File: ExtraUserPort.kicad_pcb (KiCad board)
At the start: 2 copper layers, 60.8 x 99.9 mm, 35 parts, among them CN1 EXPANSION_PORT, CN2 ALMOST_USERPORT, CN3 DB9_MALE, J1 ATTENTION_IN, J2 TAPE_IN, U1 GAL20V8, U102 74LS652, U2 MOS_6529, U3 MOS_6551_ACIA, U4 MAX238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

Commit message: wip
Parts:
- moved JP4 0.61 mm to (136.0, 90.7), turned to 0 degrees
- moved J2 0.13 mm to (129.8, 93.0)
- renumbered C5 to C4, C9 to C5
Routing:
- net /pc2: track 90.1 -> 92.8 mm
- net /pc3: track 65.1 -> 66.4 mm
- net /pc0: track 68.6 -> 69.5 mm
- net Net-(CN2-Pad9): track 30.4 -> 30.9 mm
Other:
- board text added: "↓ 6529 / 74652 ↑"
- board text removed: "↑6529 ↓74652"

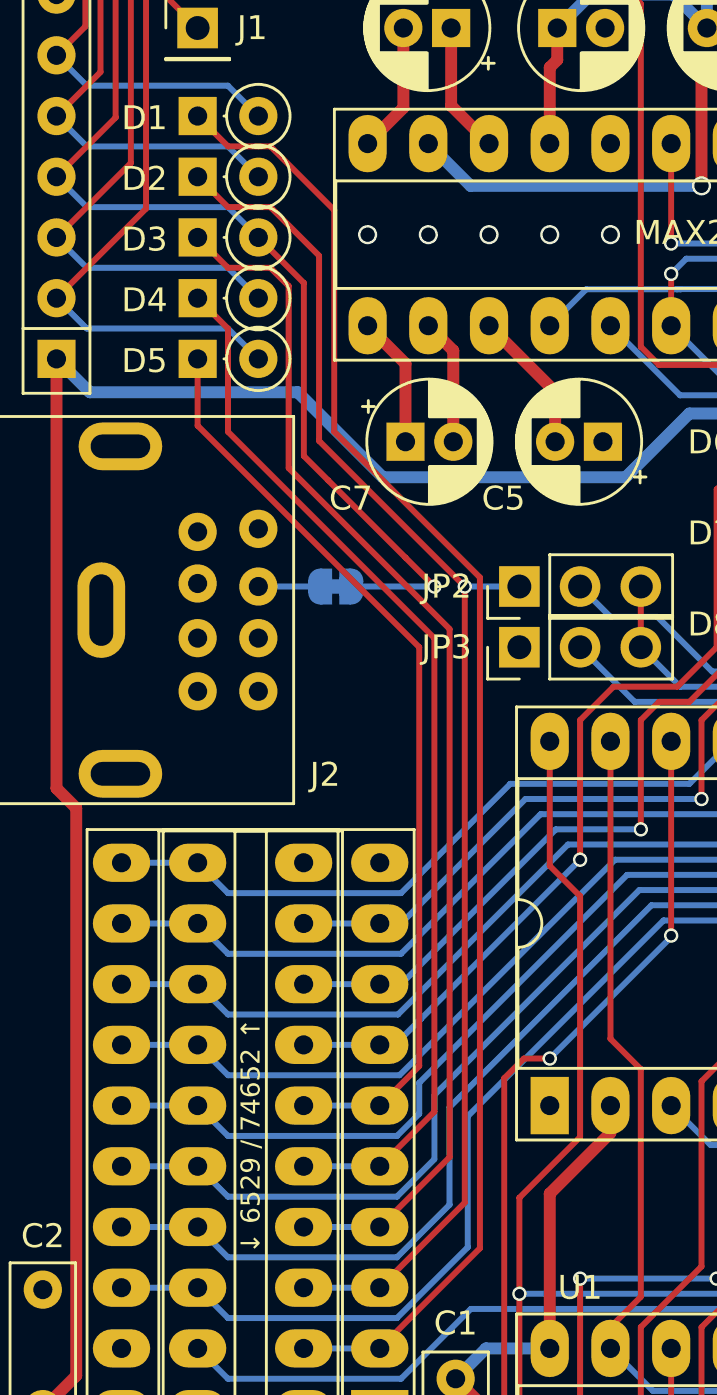
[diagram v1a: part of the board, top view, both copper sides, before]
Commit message: Move /CTS to PC2
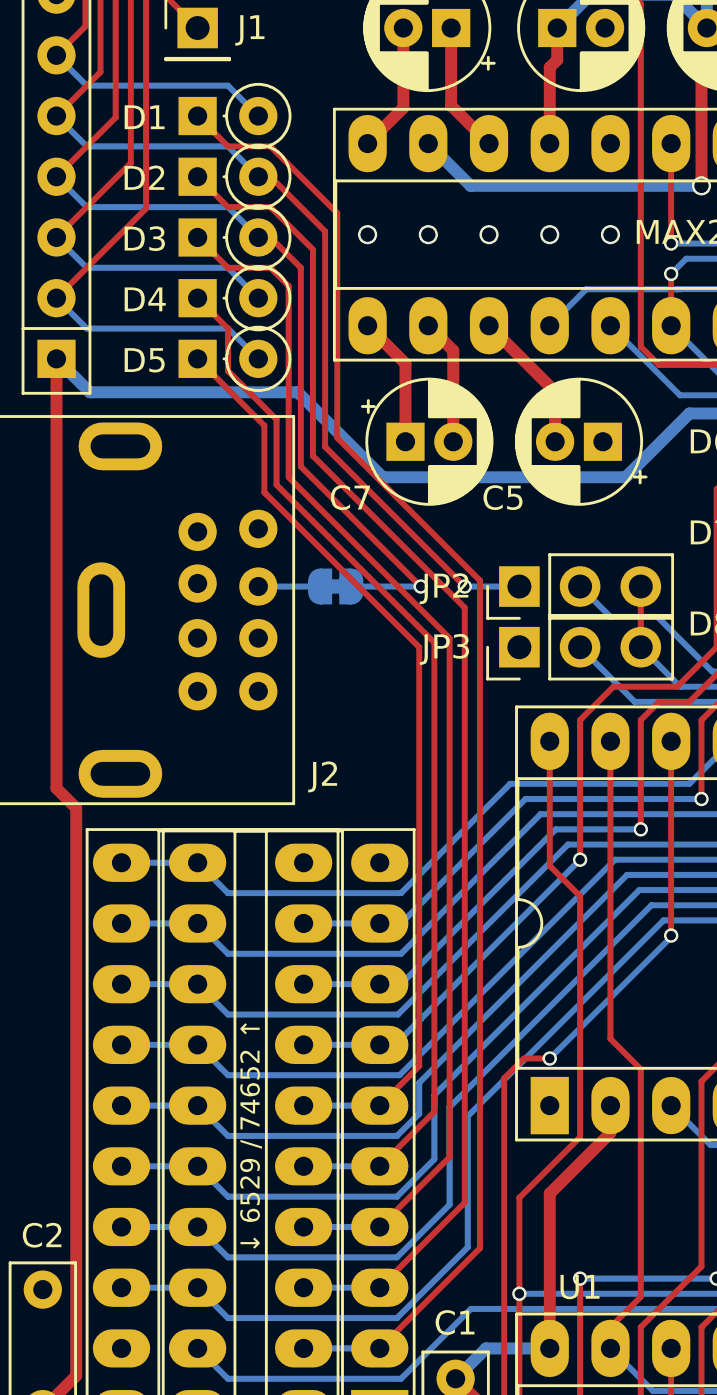
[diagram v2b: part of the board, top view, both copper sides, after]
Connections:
- JP2 pad 1: /p1 -> /pc1
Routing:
- net /pc1: track 47.4 -> 70.7 mm, vias 3 -> 4
- net /p1: track 59.1 -> 56.8 mm, vias 1 -> 0
- net /pc2: track 92.8 -> 92.3 mm

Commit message: Almost ready for prototypes
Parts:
- removed JP4: JMP_CASS_SENSE, Jumper:SolderJumper-2_P1.3mm_Bridged_RoundedPad1.0x1.5mm
- added R4: 1k, Resistor_THT:R_Axial_DIN0207_L6.3mm_D2.5mm_P2.54mm_Vertical, F.Cu at (156.3, 85.6)
- added R5: 1k, Resistor_THT:R_Axial_DIN0207_L6.3mm_D2.5mm_P2.54mm_Vertical, F.Cu at (160.1, 88.1)
- added V0: LOGO, ExtraUserPort:logo, F.Cu at (132.6, 135.6)
- added V1: CC-BY-NC-SA, ExtraUserPort:cc_by_nc_sa, B.Cu at (130.3, 135.8)
- moved D6 3.43 mm to (153.8, 88.1)
- moved D7 2.16 mm to (153.8, 90.7)
- moved R2 2.16 mm to (160.1, 90.7)
- moved D8 0.89 mm to (153.8, 93.2)
- moved R3 0.89 mm to (160.1, 93.2)
- moved R1 0.89 mm to (160.1, 85.6)
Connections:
- JP2 pad 1: /pc1 -> Net-(JP2-Pad1)
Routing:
- net /pc1: track 70.7 -> 91.9 mm
- net /~cassette_sense: track 2.59 -> 23.1 mm
- net /pc2: track 92.3 -> 110.1 mm
- net Net-(JP2-Pad1): track 0.00 -> 17.6 mm
- net +5V: track 300.0 -> 305.2 mm
- net /pc5: track 63.6 -> 68.3 mm
- net /p5: track 37.9 -> 34.4 mm
- net Net-(JP2-Pad2): track 36.8 -> 33.4 mm
- net /~dsr_ttl: track 83.3 -> 86.2 mm, vias 5 -> 6
- net Net-(JP3-Pad2): track 41.4 -> 38.7 mm
- net /pc6: track 64.9 -> 67.1 mm
- net /p6: track 31.5 -> 29.8 mm
- net /~dcd_ttl: track 95.8 -> 96.8 mm
- net /pc7: track 72.9 -> 73.6 mm
- net /~rts_ttl: track 92.9 -> 92.3 mm
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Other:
- board text added: "ADDR"
- board text added: "CC-BY-NC-SA © SukkoPera 2022 github.com/SukkoPera/16up"
- board text added: "F.C."
- board text added: "HW"
- board text added: "NOTES: - ON PLUS/4 USE EXTERNAL ADDRESS ONLY (ACIA = $FD6x, 6529 = $FD7x) - ON C16 INTERNAL ADDRESS REQUIRES MODIFICATION (ACIA = $FD0x, 6529 = $FD1x) - HW FLOW CONTROL REQUIRES W65C51S ACIA - DO NOT MOUNT RN1 IF USING ORIGINAL MOS 6529 - REPLACE D1-8 WITH 0-OHM RESISTORS IF USING ORIGINAL MOS 6529 OR 74x654 REPLACEMENT"
- board text added: "RS-232"
- board text added: "SW"
- board text removed: "ADDRESS"
- board text removed: "CC-BY-NC-SA SukkoPera 2022 github.com/SukkoPera/ExtraUserPort"

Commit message: Final touches
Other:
- board text added: "THANKS TO THE FOLKS FROM THE PLUS/4 WORLD FORUM!"
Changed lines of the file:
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@@
   (general
     (thickness 1.6)
-    (drawings 61)
+    (drawings 62)
     (tracks 937)
     (zones 0)
@@
       (xy -6.640945 2.370666) (xy 6.674813 2.370666) (xy 6.841541 2.203938)) (layer B.SilkS) (width 0.01))
   )
+  (gr_text "THANKS TO THE FOLKS FROM\nTHE PLUS/4 WORLD FORUM!" (at 158.882 126.3075) (layer B.SilkS)
+    (effects (font (size 1 1) (thickness 0.15)) (justify mirror))
+  )
   (gr_text RS-232 (at 169.164 75.946001 90) (layer F.SilkS)
     (effects (font (size 1 1) (thickness 0.15)))
@@
   (segment (start 134.493 85.6615) (end 138.84275 90.01125) (width 0.25) (layer F.Cu) (net 73))
   (via (at 138.84275 90.01125) (size 0.6) (drill 0.4) (layers F.Cu B.Cu) (net 73))
-  (segment (start 149.352 87.503) (end 141.351 87.503) (width 0.25) (layer B.Cu) (net 73))
-  (segment (start 152.654 84.201) (end 149.352 87.503) (width 0.25) (layer B.Cu) (net 73))
   (segment (start 141.351 87.503) (end 138.84275 90.01125) (width 0.25) (layer B.Cu) (net 73))
-  (segment (start 154.870685 84.201) (end 152.654 84.201) (width 0.25) (layer B.Cu) (net 73))
-  (segment (start 156.267685 85.598) (end 154.870685 84.201) (width 0.25) (layer B.Cu) (net 73) (status 10))
+  (segment (start 152.527 84.328) (end 149.352 87.503) (width 0.25) (layer B.Cu) (net 73))
+  (segment (start 154.997685 84.328) (end 152.527 84.328) (width 0.25) (layer B.Cu) (net 73))
+  (segment (start 149.352 87.503) (end 141.351 87.503) (width 0.25) (layer B.Cu) (net 73))
+  (segment (start 156.267685 85.598) (end 154.997685 84.328) (width 0.25) (layer B.Cu) (net 73))
   (via (at 149.987 125.095) (size 0.6) (drill 0.4) (layers F.Cu B.Cu) (net 74))
   (segment (start 149.987 125.095) (end 149.987 122.555) (width 0.25) (layer F.Cu) (net 74) (status 20))
@@
       )
     )
+  )
+  (zone (net 0) (net_name "") (layer B.Cu) (hatch edge 0.508)
+    (connect_pads (clearance 0.381))
+    (min_thickness 0.254)
+    (keepout (tracks allowed) (vias allowed) (copperpour not_allowed))
+    (fill (arc_segments 32) (thermal_gap 0.508) (thermal_bridge_width 0.508))
+    (polygon
+      (pts
+        (xy 133.35 126.761883) (xy 133.35 128.412883) (xy 135.763 128.412883) (xy 135.763 126.761883)
+      )
+    )
